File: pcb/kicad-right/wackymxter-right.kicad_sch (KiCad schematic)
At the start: 82 parts, among them J1 OLED_128x32, J2 Conn_01x03, U1 Pico, U3 TRRS

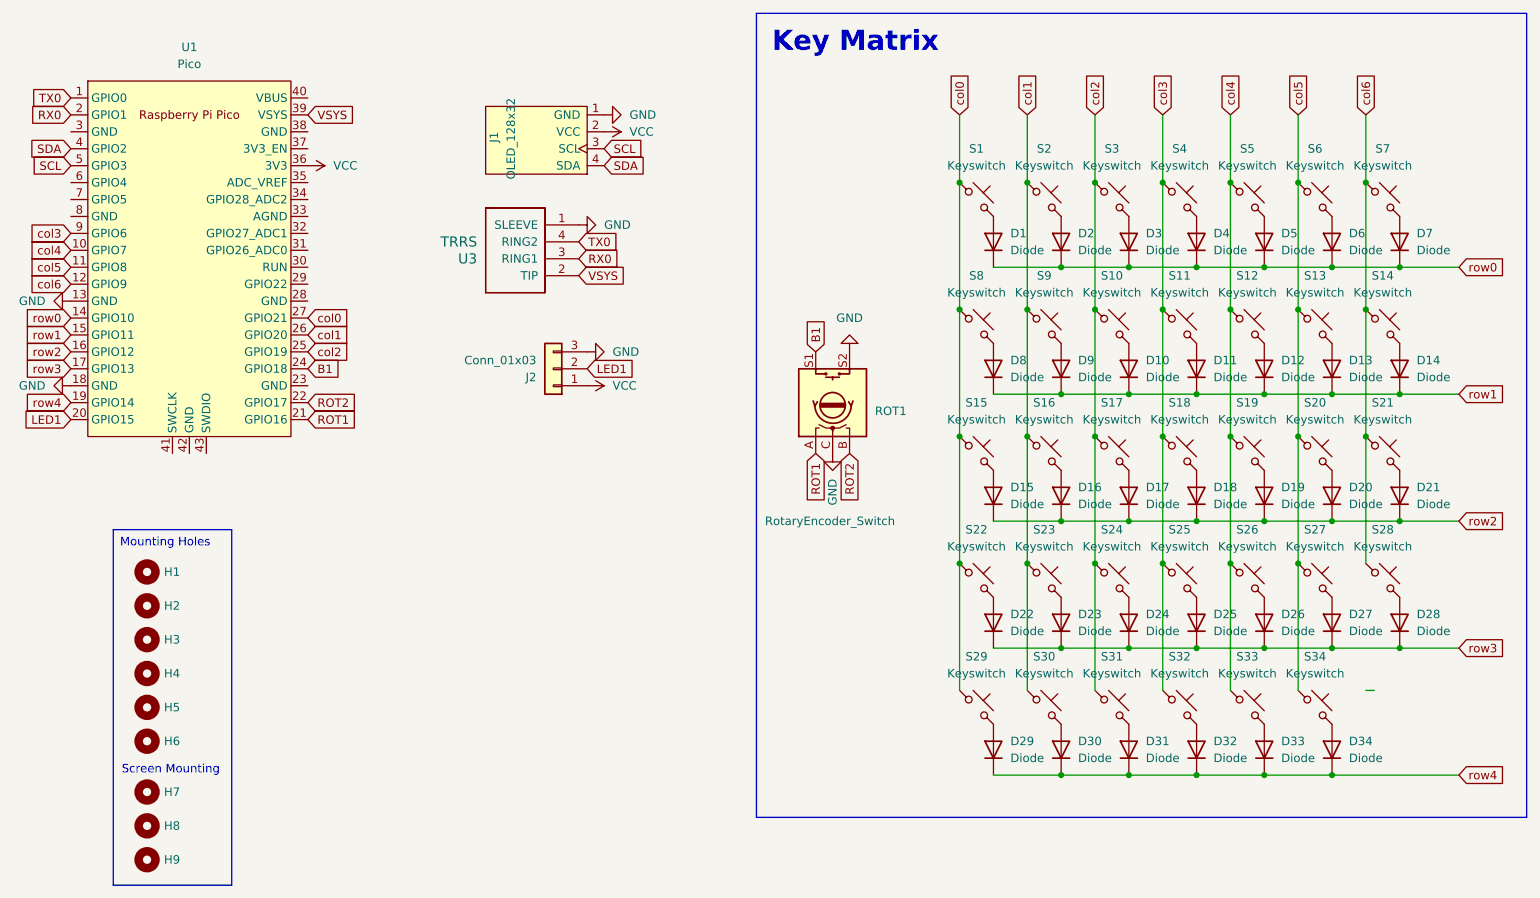
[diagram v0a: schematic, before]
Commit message: [KiCAD] draft of left and right with 1.5u and fully connected
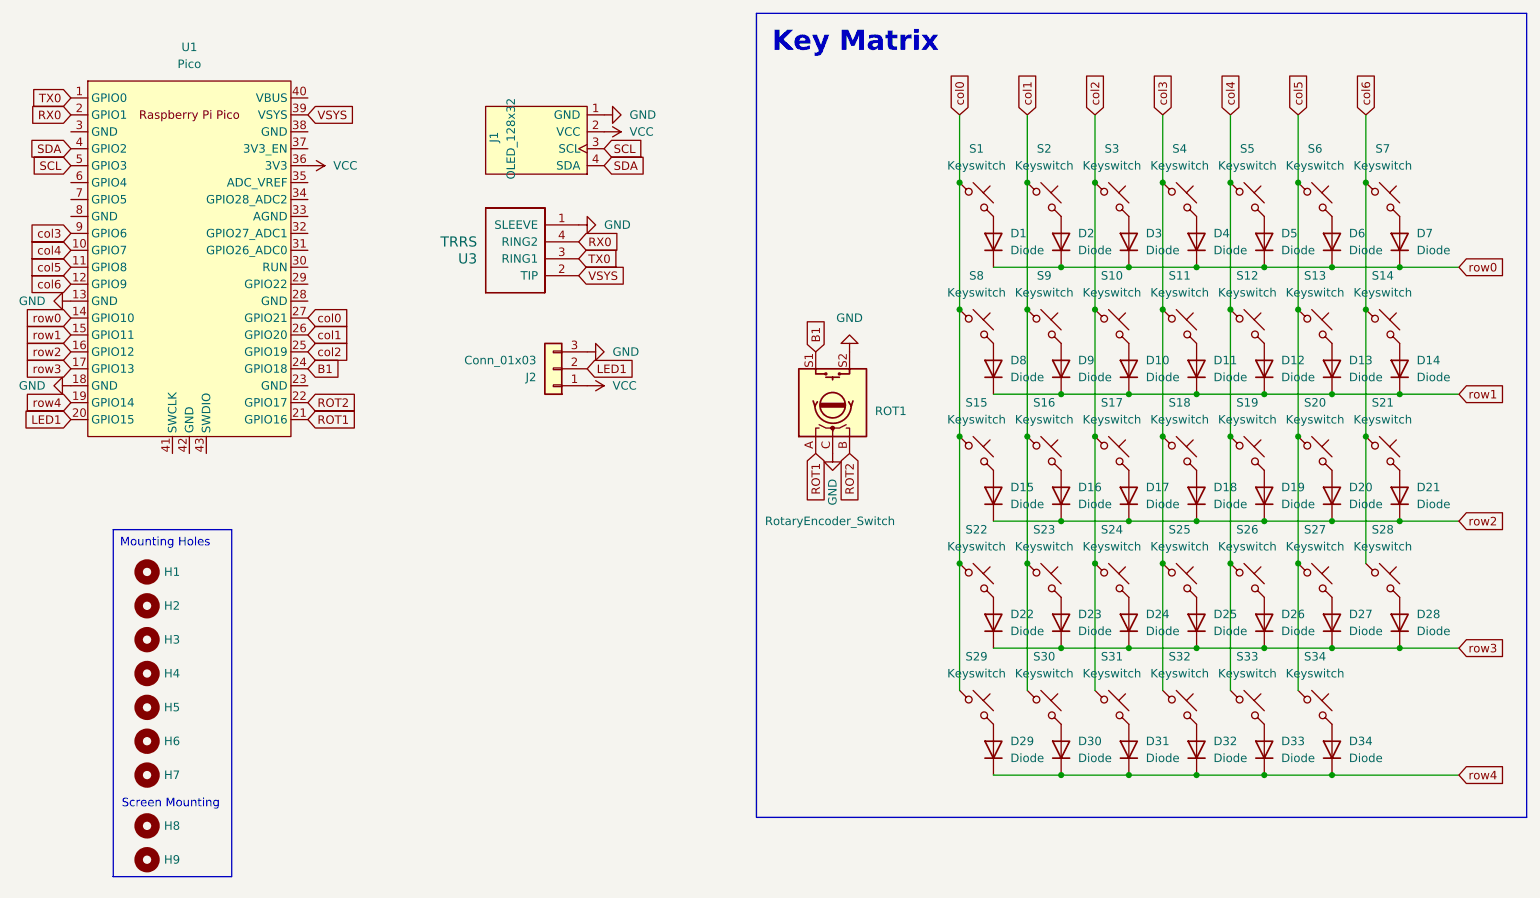
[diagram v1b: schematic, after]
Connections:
- net RX0: now also U3.4 (RING2); no longer U3.3 (RING1)
- net TX0: now also U3.3 (RING1); no longer U3.4 (RING2)
